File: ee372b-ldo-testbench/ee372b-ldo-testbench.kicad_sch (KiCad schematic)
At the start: 128 parts, among them J1 PEC02SAAN, J10 OUT_S, J11 VOUT, J12 VDD_BUF, J13 V_SIG, J14 PEC03SAAN, J15 VSIG_BUF, J16 PEC03SAAN, J17 PEC03SAAN, J18 PEC03SAAN, J19 PEC03SAAN, J2 PEC02SAAN, J20 VREF_EXTERNAL, J21 PEC02SAAN, J22 PEC02SAAN, J23 PEC02SAAN, J24 PEC02SAAN, J25 PEC03SAAN, J3 GND, J4 1V8, J5 3v3_EXTERNAL, J6 GND, J9 IN_S, Q1 FDV305N, Q2 FDV305N, Q3 FDV305N, Q4 FDV305N, Q5 FDV305N, U1 MMSZ4679T1G, U3 ADS1220IPW, U4 BUF634AIDR

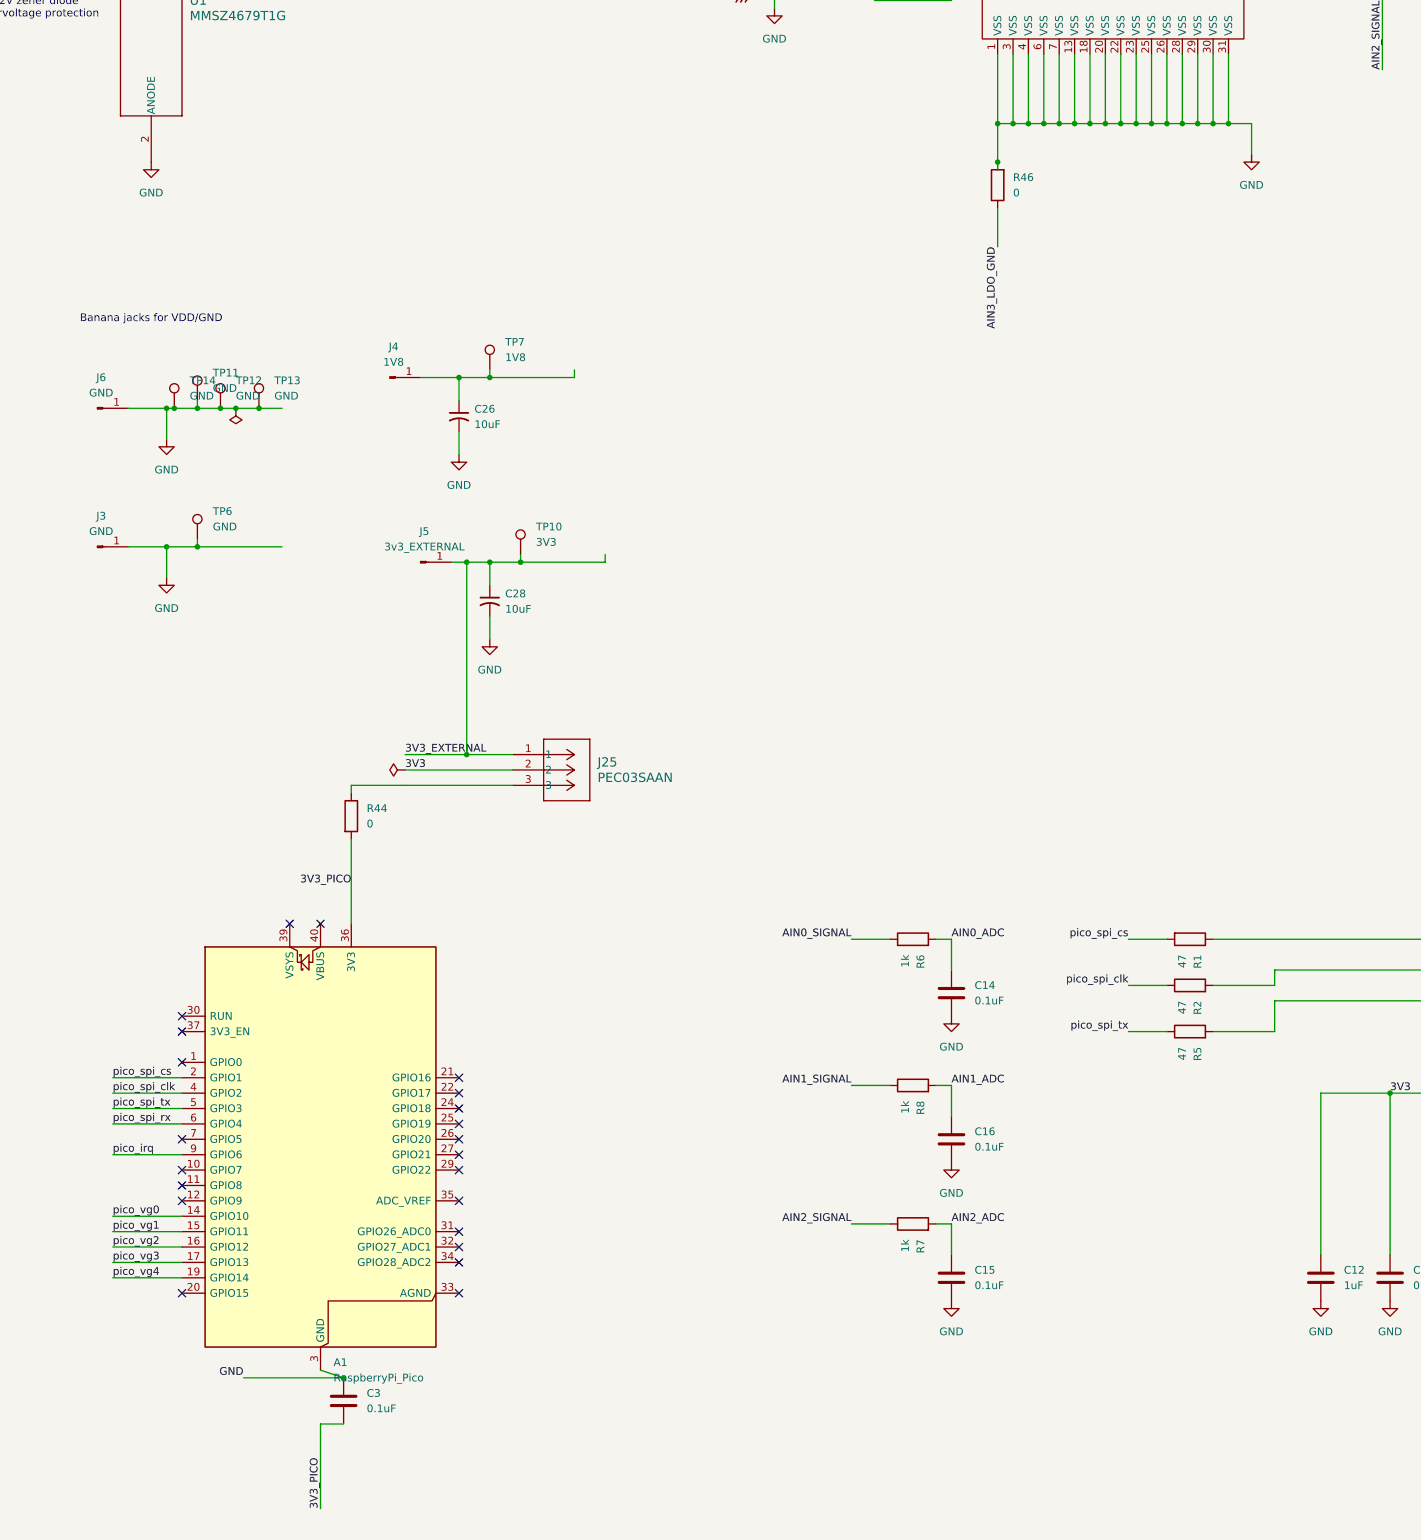
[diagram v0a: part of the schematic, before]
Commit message: otuput bank traces thicker
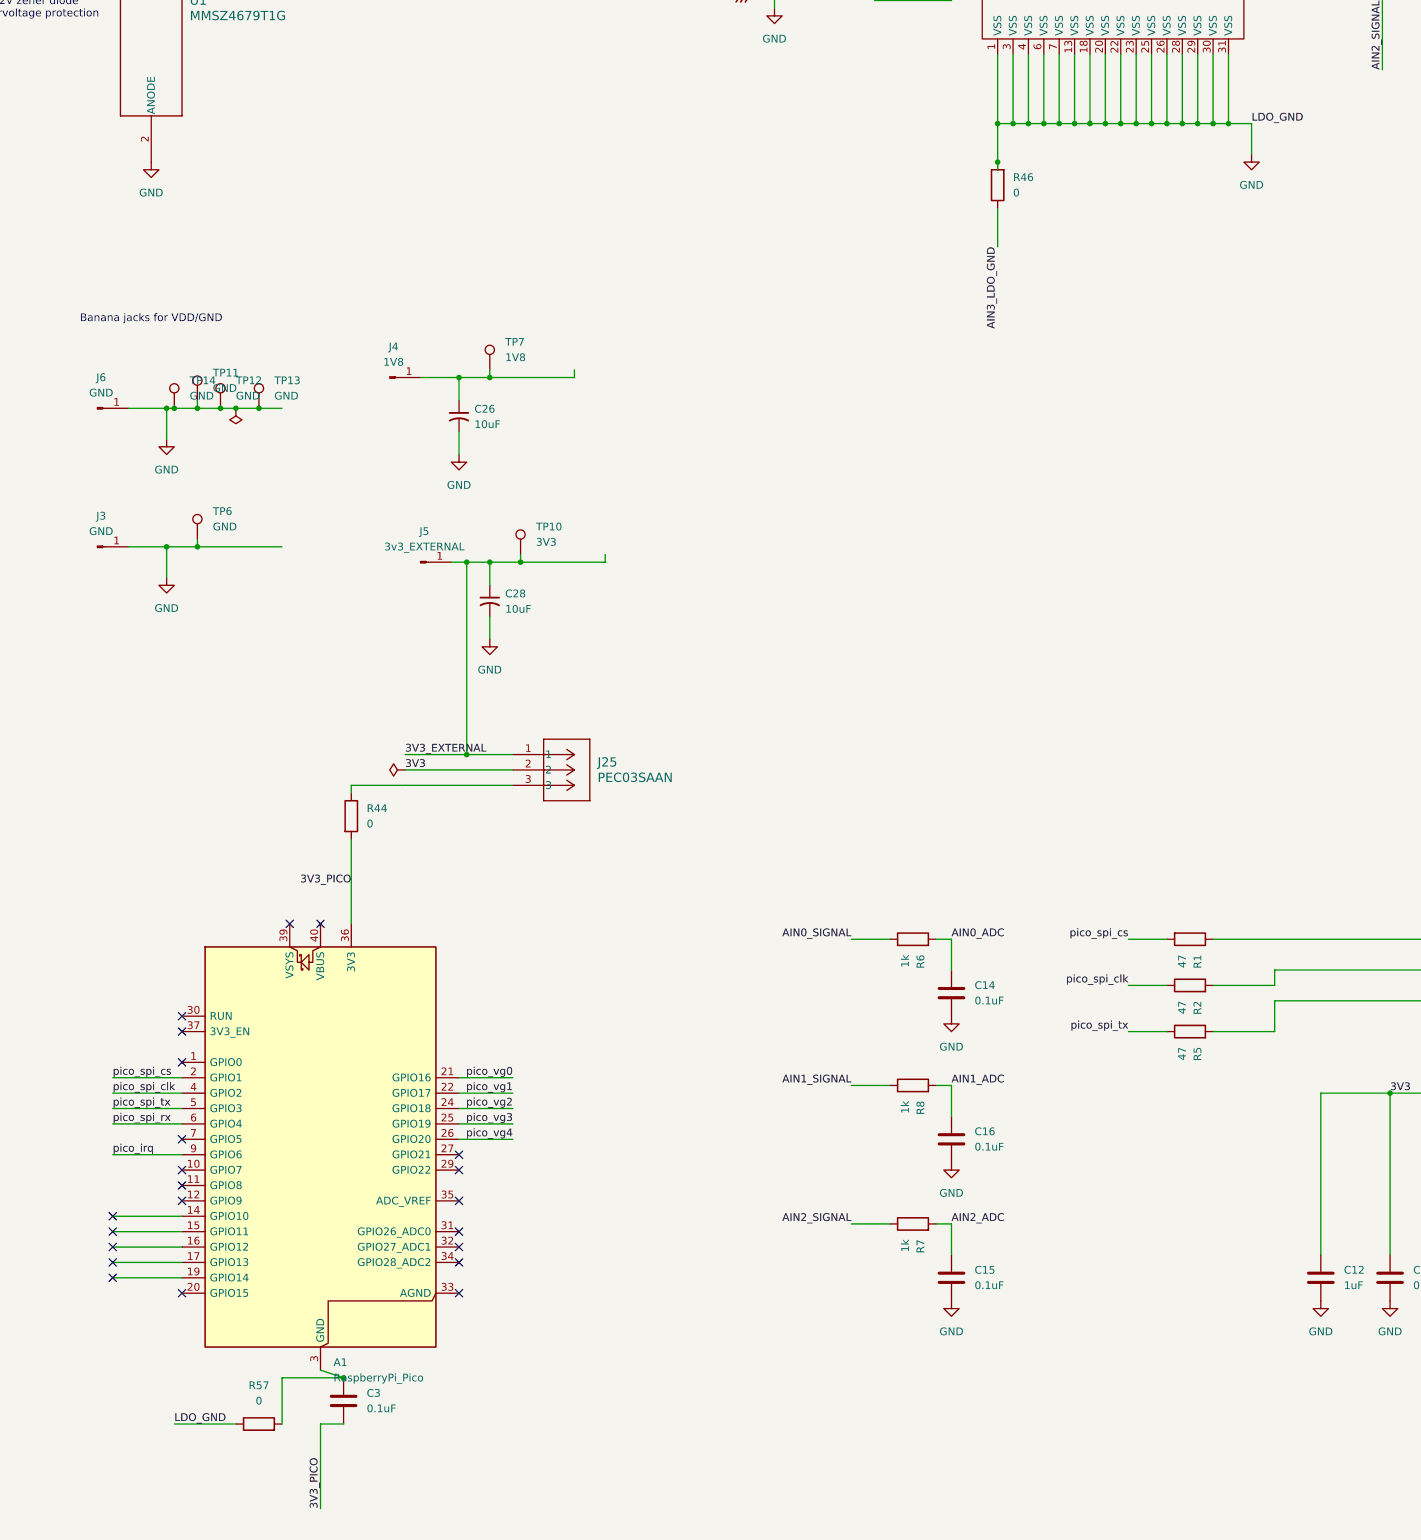
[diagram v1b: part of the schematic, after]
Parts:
- added R57: 0, Resistor_SMD:R_0805_2012Metric_Pad1.20x1.40mm_HandSolder, symbol Device:R
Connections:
- net GND: now also R57.1; no longer A1.13 (GND), A1.18 (GND), A1.23 (GND), A1.28 (GND), A1.3 (GND), A1.38 (GND), A1.8 (GND), C3.1
- net pico_vg0: now also A1.21 (GPIO16); no longer A1.14 (GPIO10)
- net pico_vg1: now also A1.22 (GPIO17); no longer A1.15 (GPIO11)
- net pico_vg2: now also A1.24 (GPIO18); no longer A1.16 (GPIO12)
- net pico_vg3: now also A1.25 (GPIO19); no longer A1.17 (GPIO13)
- net pico_vg4: now also A1.26 (GPIO20); no longer A1.19 (GPIO14)
- new net: A1.13 (GND), A1.18 (GND), A1.23 (GND), A1.28 (GND), A1.3 (GND), A1.38 (GND), A1.8 (GND), C3.1, R57.2
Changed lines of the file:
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@@
 	)
 	(no_connect
-		(at 255.27 295.91)
+		(at 255.27 306.07)
 	)
 	(no_connect
@@
 	)
 	(no_connect
-		(at 255.27 293.37)
+		(at 198.12 316.23)
 	)
 	(no_connect
@@
 	)
 	(no_connect
-		(at 255.27 300.99)
-	)
-	(no_connect
 		(at 255.27 318.77)
 	)
@@
 	)
 	(no_connect
+		(at 198.12 321.31)
+	)
+	(no_connect
 		(at 209.55 313.69)
 	)
@@
 	)
 	(no_connect
-		(at 209.55 285.75)
+		(at 198.12 326.39)
 	)
 	(no_connect
-		(at 209.55 328.93)
+		(at 209.55 285.75)
 	)
 	(no_connect
-		(at 255.27 328.93)
+		(at 209.55 328.93)
 	)
 	(no_connect
-		(at 255.27 298.45)
+		(at 198.12 323.85)
 	)
 	(no_connect
-		(at 209.55 308.61)
+		(at 198.12 318.77)
 	)
 	(no_connect
-		(at 255.27 308.61)
+		(at 255.27 328.93)
 	)
 	(no_connect
-		(at 255.27 303.53)
+		(at 209.55 308.61)
 	)
 	(no_connect
-		(at 255.27 306.07)
+		(at 255.27 308.61)
 	)
 	(no_connect
@@
 	(wire
 		(pts
+			(xy 208.28 350.52) (xy 218.44 350.52)
+		)
+		(stroke
+			(width 0)
+			(type default)
+		)
+	)
+	(wire
+		(pts
 			(xy 367.03 135.89) (xy 369.57 135.89)
 		)
@@
 	(wire
 		(pts
+			(xy 226.06 342.9) (xy 226.06 350.52)
+		)
+		(stroke
+			(width 0)
+			(type default)
+		)
+	)
+	(wire
+		(pts
 			(xy 82.55 290.83) (xy 88.9 290.83)
 		)
@@
 	(wire
 		(pts
+			(xy 255.27 298.45) (xy 264.16 298.45)
+		)
+		(stroke
+			(width 0)
+			(type default)
+		)
+	)
+	(wire
+		(pts
 			(xy 364.49 80.01) (xy 364.49 83.82)
 		)
@@
 	(wire
 		(pts
+			(xy 264.16 295.91) (xy 255.27 295.91)
+		)
+		(stroke
+			(width 0)
+			(type default)
+		)
+	)
+	(wire
+		(pts
 			(xy 88.9 280.67) (xy 104.14 280.67)
 		)
@@
 	(wire
 		(pts
+			(xy 255.27 303.53) (xy 264.16 303.53)
+		)
+		(stroke
+			(width 0)
+			(type default)
+		)
+	)
+	(wire
+		(pts
 			(xy 68.58 280.67) (xy 88.9 280.67)
 		)
@@
 	(wire
 		(pts
-			(xy 219.71 342.9) (xy 236.22 342.9)
-		)
-		(stroke
-			(width 0)
-			(type default)
-		)
-	)
-	(wire
-		(pts
 			(xy 82.55 114.3) (xy 86.36 114.3)
 		)
@@
 	(wire
 		(pts
+			(xy 255.27 293.37) (xy 264.16 293.37)
+		)
+		(stroke
+			(width 0)
+			(type default)
+		)
+	)
+	(wire
+		(pts
 			(xy 36.83 199.39) (xy 38.1 199.39)
 		)
@@
 	(wire
 		(pts
+			(xy 226.06 342.9) (xy 236.22 342.9)
+		)
+		(stroke
+			(width 0)
+			(type default)
+		)
+	)
+	(wire
+		(pts
 			(xy 207.01 205.74) (xy 200.66 205.74)
 		)
@@
 	(wire
 		(pts
+			(xy 255.27 300.99) (xy 264.16 300.99)
+		)
+		(stroke
+			(width 0)
+			(type default)
+		)
+	)
+	(wire
+		(pts
 			(xy 379.73 135.89) (xy 382.27 135.89)
 		)
@@
 	)
 	(label "pico_vg4"
-		(at 198.12 326.39 0)
+		(at 264.16 303.53 180)
 		(effects
 			(font
 				(size 1.27 1.27)
 			)
-			(justify left bottom)
+			(justify right bottom)
 		)
 	)
@@
 	)
 	(label "pico_vg0"
-		(at 198.12 316.23 0)
+		(at 264.16 293.37 180)
 		(effects
 			(font
 				(size 1.27 1.27)
 			)
-			(justify left bottom)
+			(justify right bottom)
 		)
 	)
@@
 		)
 	)
+	(label "LDO_GND"
+		(at 386.08 135.89 0)
+		(effects
+			(font
+				(size 1.27 1.27)
+			)
+			(justify left bottom)
+		)
+	)
 	(label "VG3"
 		(at 120.65 370.84 180)
@@
 		)
 	)
-	(label "pico_vg2"
-		(at 198.12 321.31 0)
+	(label "c2_vin_jump"
+		(at 31.75 81.28 180)
 		(effects
 			(font
 				(size 1.27 1.27)
 			)
-			(justify left bottom)
+			(justify right bottom)
 		)
 	)
-	(label "c2_vin_jump"
-		(at 31.75 81.28 180)
+	(label "LDO_GND"
+		(at 208.28 350.52 0)
 		(effects
 			(font
 				(size 1.27 1.27)
 			)
-			(justify right bottom)
+			(justify left bottom)
 		)
 	)
@@
 		)
 	)
+	(label "pico_vg2"
+		(at 264.16 298.45 180)
+		(effects
+			(font
+				(size 1.27 1.27)
+			)
+			(justify right bottom)
+		)
+	)
 	(label "c2_vout_jump"
 		(at 464.82 101.6 90)
@@
 	)
 	(label "pico_vg3"
-		(at 198.12 323.85 0)
+		(at 264.16 300.99 180)
 		(effects
 			(font
 				(size 1.27 1.27)
 			)
-			(justify left bottom)
+			(justify right bottom)
 		)
 	)
@@
 		)
 	)
-	(label "GND"
-		(at 219.71 342.9 180)
-		(effects
-			(font
-				(size 1.27 1.27)
-			)
-			(justify right bottom)
-		)
-	)
 	(label "VG4"
 		(at 124.46 299.72 0)
@@
 	)
 	(label "pico_vg1"
-		(at 198.12 318.77 0)
+		(at 264.16 295.91 180)
 		(effects
 			(font
 				(size 1.27 1.27)
 			)
-			(justify left bottom)
+			(justify right bottom)
 		)
 	)
@@
 					(unit 1)
 				)
+			)
+		)
+	)
+	(symbol
+		(lib_id "Device:R")
+		(at 222.25 350.52 90)
+		(unit 1)
+		(body_style 1)
+		(exclude_from_sim no)
+		(in_bom yes)
+		(on_board yes)
+		(in_pos_files yes)
+		(dnp no)
+		(fields_autoplaced yes)
+		(property "Reference" "R57"
+			(at 222.25 344.17 90)
+			(show_name no)
+			(do_not_autoplace no)
+			(effects
+				(font
+					(size 1.27 1.27)
+				)
+			)
+		)
+		(property "Value" "0"
+			(at 222.25 346.71 90)
+			(show_name no)
+			(do_not_autoplace no)
+			(effects
+				(font
+					(size 1.27 1.27)
+				)
+			)
+		)
+		(property "Footprint" "Resistor_SMD:R_0805_2012Metric_Pad1.20x1.40mm_HandSolder"
+			(at 222.25 352.298 90)
+			(hide yes)
+			(show_name no)
+			(do_not_autoplace no)
+			(effects
+				(font
+					(size 1.27 1.27)
+				)
+			)
+		)
+		(property "Datasheet" "https://www.vishay.com/docs/20043/crcwhpe3.pdf"
+			(at 222.25 350.52 0)
+			(hide yes)
+			(show_name no)
+			(do_not_autoplace no)
+			(effects
+				(font
+					(size 1.27 1.27)
+				)
+			)
+		)
+		(property "Description" "RES SMD 0 OHM JUMPER 1/2W 0805"
+			(at 222.25 350.52 0)
+			(hide yes)
+			(show_name no)
+			(do_not_autoplace no)
+			(effects
+				(font
+					(size 1.27 1.27)
+				)
+			)
+		)
+		(property "Manufacturer" "Vishay Dale"
+			(at 222.25 350.52 0)
+			(hide yes)
+			(show_name no)
+			(do_not_autoplace no)
+			(effects
+				(font
+					(size 1.27 1.27)
+				)
+			)
+		)
+		(property "Manufacturer Part Number" "CRCW08050000Z0EAHP"
+			(at 222.25 350.52 0)
+			(hide yes)
+			(show_name no)
+			(do_not_autoplace no)
+			(effects
+				(font
+					(size 1.27 1.27)
+				)
+			)
+		)
+		(property "Distributer Link 1" "https://www.digikey.com/en/products/detail/vishay-dale/CRCW08050000Z0EAHP/2222316"
+			(at 222.25 350.52 0)
+			(hide yes)
+			(show_name no)
+			(do_not_autoplace no)
+			(effects
+				(font
+					(size 1.27 1.27)
+				)
+			)
+		)
+		(property "Distrbuter Link 2" "https://www.mouser.com/en/ProductDetail/Vishay/CRCW08050000Z0EAHP?qs=pTGEtN%252BMLlDLrJUqQmN2jA%3D%3D"
+			(at 222.25 350.52 0)
+			(hide yes)
+			(show_name no)
+			(do_not_autoplace no)
+			(effects
+				(font
+					(size 1.27 1.27)
+				)
+			)
+		)
+		(pin "2"
+		)
+		(pin "1"
+		)
+		(instances
+			(project "ee372b-ldo-testbench"
+				(path "/4eaac8a8-2761-424f-b17c-d4cc8c253812"
+					(reference "R57")
+					(unit 1)
+				)

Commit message: finished thcicker traces whole board
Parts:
- removed R38, R39, R41, R9: 0, Resistor_SMD:R_0805_2012Metric_Pad1.20x1.40mm_HandSolder, symbol Device:R
- R40, R42, R43, R61: now not fitted
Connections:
- net GND: now also R42.1, R61.1; no longer C20.2, C21.2, C22.2, C25.2
- net LDO_VOUT: now also J21.1, J22.1, J23.1, J24.1; no longer R42.1, R61.1
- net at R61.2: now also C20.2; no longer J23.1
- net at C25.1, J24.2: no longer R43.2
- net at C22.1, J23.2: no longer R40.2
- net at R42.2: now also C25.2; no longer J24.1
- new net: C22.2, R40.2
- new net: C21.2, R43.2

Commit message: emailed to TAs
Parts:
- R37, R44, R45, R46, R47, R48, R49, R55, R57, R58, R60, R62, R64: now not fitted
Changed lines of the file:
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@@
 		(on_board yes)
 		(in_pos_files yes)
-		(dnp no)
+		(dnp yes)
 		(fields_autoplaced yes)
 		(property "Reference" "R60"
@@
 		(on_board yes)
 		(in_pos_files yes)
-		(dnp no)
+		(dnp yes)
 		(fields_autoplaced yes)
 		(property "Reference" "R49"
@@
 		(on_board yes)
 		(in_pos_files yes)
-		(dnp no)
+		(dnp yes)
 		(fields_autoplaced yes)
 		(property "Reference" "R44"
@@
 		(on_board yes)
 		(in_pos_files yes)
-		(dnp no)
+		(dnp yes)
 		(fields_autoplaced yes)
 		(property "Reference" "R46"
@@
 		(on_board yes)
 		(in_pos_files yes)
-		(dnp no)
+		(dnp yes)
 		(fields_autoplaced yes)
 		(property "Reference" "R55"
@@
 		(on_board yes)
 		(in_pos_files yes)
-		(dnp no)
+		(dnp yes)
 		(fields_autoplaced yes)
 		(property "Reference" "R47"
@@
 		(on_board yes)
 		(in_pos_files yes)
-		(dnp no)
+		(dnp yes)
 		(fields_autoplaced yes)
 		(property "Reference" "R62"
@@
 		(on_board yes)
 		(in_pos_files yes)
-		(dnp no)
+		(dnp yes)
 		(fields_autoplaced yes)
 		(property "Reference" "R58"
@@
 		(on_board yes)
 		(in_pos_files yes)
-		(dnp no)
+		(dnp yes)
 		(fields_autoplaced yes)
 		(property "Reference" "R48"
@@
 		(on_board yes)
 		(in_pos_files yes)
-		(dnp no)
+		(dnp yes)
 		(fields_autoplaced yes)
 		(property "Reference" "R57"
@@
 		(on_board yes)
 		(in_pos_files yes)
-		(dnp no)
+		(dnp yes)
 		(fields_autoplaced yes)
 		(property "Reference" "R37"
@@
 		(on_board yes)
 		(in_pos_files yes)
-		(dnp no)
+		(dnp yes)
 		(fields_autoplaced yes)
 		(property "Reference" "R45"
@@
 		(on_board yes)
 		(in_pos_files yes)
-		(dnp no)
+		(dnp yes)
 		(fields_autoplaced yes)
 		(property "Reference" "R64"

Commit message: forgot drill files last time
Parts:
- removed TP14: GND, 1_EE372_DemoBoard:KEYSTONE_5016, symbol Connector:TestPoint
- added TP14, TP17: TestPoint_Probe, TestPoint:TestPoint_Pad_D1.0mm, symbol Connector:TestPoint_Probe
- added TP15, TP16: GND, 1_EE372_DemoBoard:KEYSTONE_5016, symbol Connector:TestPoint
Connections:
- net 1V8: now also TP14.1
- net GND: now also TP15.1, TP16.1
- net c1_vin_jump: now also TP17.1
